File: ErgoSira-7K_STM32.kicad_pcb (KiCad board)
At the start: 2 copper layers, 136.5 x 87.3 mm, 25 parts, among them SW2 SW_Push, U1 XC6206PxxxMR, U2 STM32G431KBTx, U3 USBLC6-2SC6

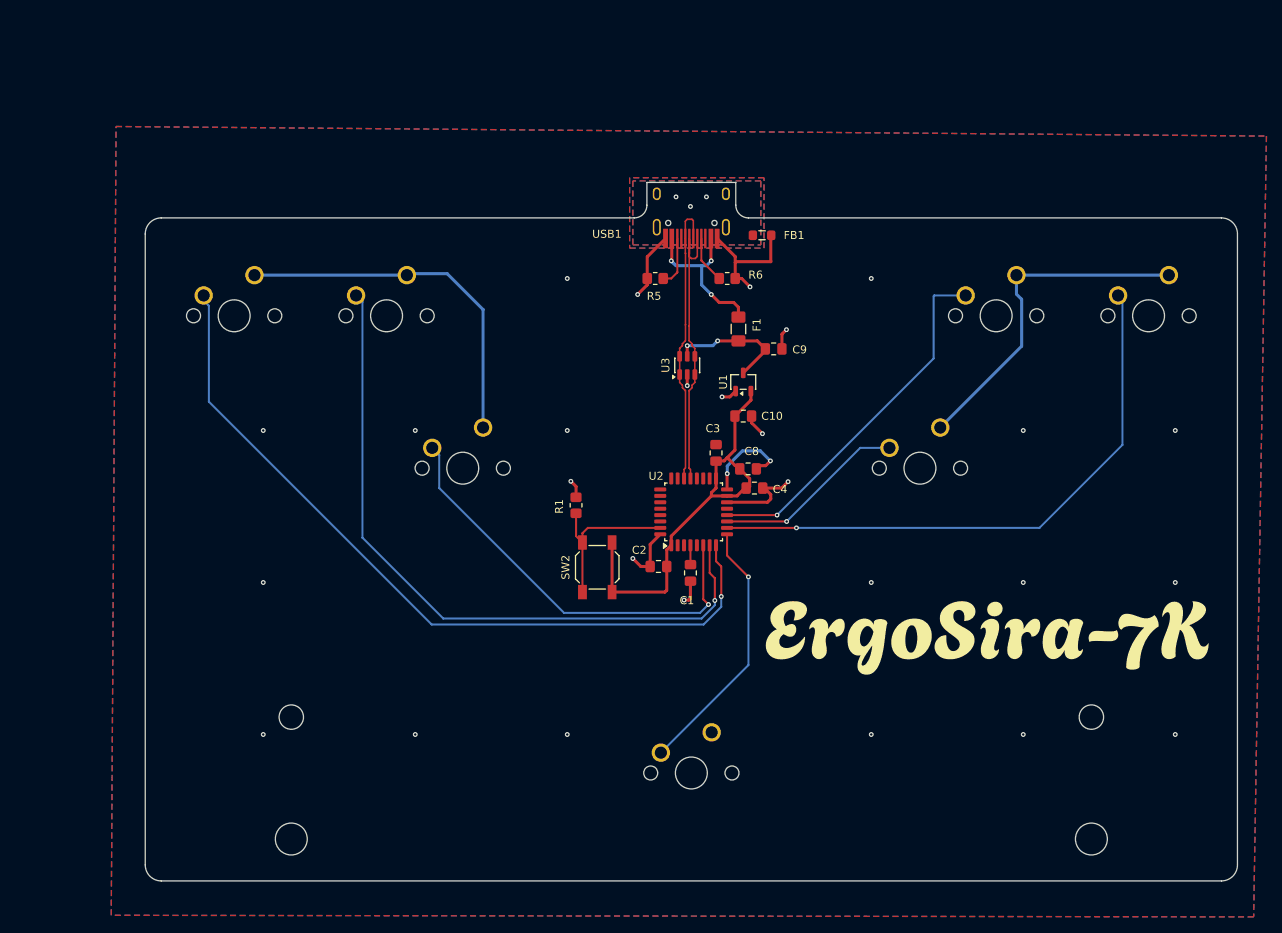
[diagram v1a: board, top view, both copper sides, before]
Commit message: fixed stabilizers orientation. added graphics
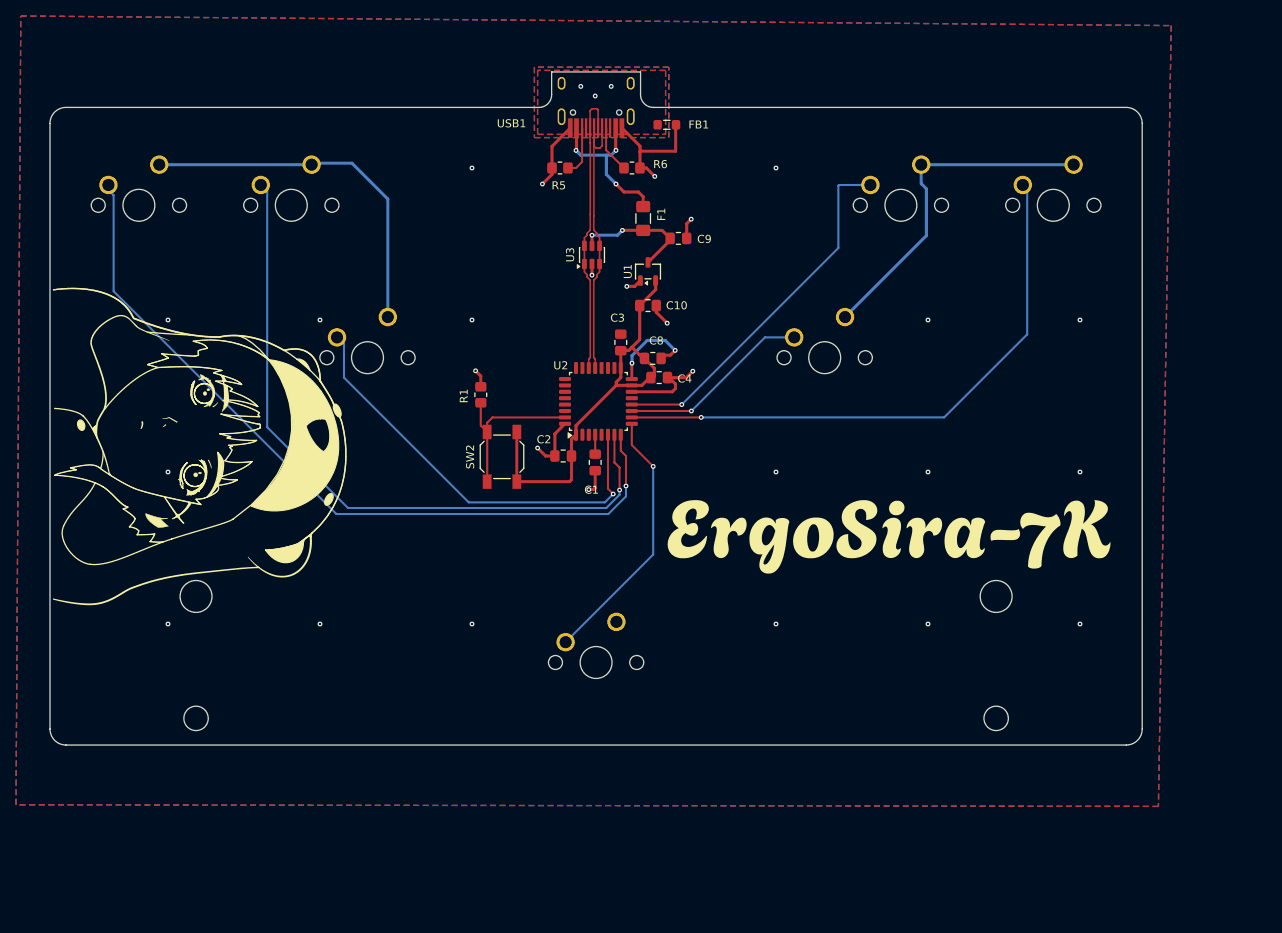
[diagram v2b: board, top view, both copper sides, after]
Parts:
- moved C1 18.2 mm to (151.5, 102.0)
- moved C10 18.2 mm to (158.1, 82.4)
- moved C2 18.2 mm to (147.5, 101.2)
- moved C3 18.2 mm to (154.7, 87.0)
- moved C4 18.2 mm to (159.5, 91.4)
- moved C8 18.2 mm to (158.7, 89.0)
- moved C9 18.2 mm to (161.9, 74.0)
- moved F1 18.2 mm to (157.5, 71.5)
- moved MX1 18.2 mm to (94.5, 69.8)
- moved MX2 18.2 mm to (113.5, 69.8)
- moved MX3 18.2 mm to (123.0, 88.9)
- moved MX4 18.2 mm to (180.2, 88.9)
- moved MX5 18.2 mm to (189.7, 69.8)
- moved MX6 18.2 mm to (208.8, 69.8)
- moved MX7 18.2 mm to (151.6, 127.0)
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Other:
- board size 136.5 x 87.3 mm -> 136.5 x 84.1 mm

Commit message: idk
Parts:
- removed S1: MX_stab, marbastlib-mx:STAB_MX_6.25u
- added MX8: MX_SW_solder, marbastlib-mx:SW_MX_1u, F.Cu at (180.2, 127.0)
- moved MX7 28.6 mm to (123.0, 127.0)
- moved R1 13.7 mm to (135.8, 107.2), turned to 180 degrees
- moved C9 1.09 mm to (160.8, 74.0)
- moved C2 0.39 mm to (147.5, 100.8)
- moved C1 0.19 mm to (151.5, 101.8)
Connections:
- U2 pad 26: unconnected-(U2-PB3-Pad26) -> SW2
- U2 pad 27: unconnected-(U2-PB4-Pad27) -> SW1
- U2 pad 28: unconnected-(U2-PB5-Pad28) -> SW3
- U2 pad 6: SW3 -> unconnected-(U2-PA1-Pad6)
- U2 pad 7: SW2 -> SW7
- U2 pad 8: SW1 -> SW8
- U2 pad 9: SW7 -> unconnected-(U2-PA4-Pad9)
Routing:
- net GND: track 156.4 -> 65.4 mm, vias 29 -> 26
- net SW2: track 87.3 -> 49.8 mm, vias 1 -> 0
- net SW8: track 0.00 -> 34.9 mm
- net SW1: track 98.9 -> 71.4 mm, vias 1 -> 0
- net SW3: track 53.7 -> 33.2 mm, vias 1 -> 0
- net SW7: track 32.9 -> 49.6 mm, vias 1 -> 0
- net +5V: track 15.9 -> 14.3 mm
- net SW6: vias 1 -> 0
- net SW5: vias 1 -> 0
- net SW4: vias 1 -> 0
